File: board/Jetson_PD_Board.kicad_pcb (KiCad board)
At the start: 2 copper layers, 100 x 100.5 mm, 28 parts, among them J1 USB4081-03-A, J2 768250002, Q1 NTTFS5C673NLTAG, Q2 NTTFS5C673NLTAG, Q3 NTTFS5C673NLTAG, U1 APK43070DKZ-13-FA01, U2 USBLC6-2SC6

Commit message: Fixed 3D model file path
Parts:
- moved C7 233.8 mm to (54.0, 265.0)
- moved C8 227.8 mm to (54.1, 261.5)
- moved TH1 224.8 mm to (54.5, 256.5)
- moved R10 221.8 mm to (54.5, 251.0)
- moved R9 219.8 mm to (54.6, 246.5)
- moved R8 217.8 mm to (54.5, 242.0)
- moved C5 211.6 mm to (41.1, 238.5)
- moved C6 211.6 mm to (41.1, 241.0)
- moved R2 211.1 mm to (54.9, 237.5)
- moved C10 209.1 mm to (54.5, 233.0)
- moved C9 206.6 mm to (54.4, 228.0)
- moved R3 205.0 mm to (39.1, 234.5)
- moved C3 202.0 mm to (54.0, 223.0)
- moved R4 201.1 mm to (33.0, 233.0)
- moved C4 194.5 mm to (54.0, 218.0)
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
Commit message: Fixed 3d all 3D model file paths
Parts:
- U1: moved to F.Cu
- moved C7 199.1 mm to (143.5, 87.1)
- moved TH1 195.5 mm to (152.2, 87.1)
- moved C8 193.7 mm to (143.5, 89.6)
- moved R10 192.9 mm to (152.2, 84.6)
- moved R9 191.2 mm to (152.2, 82.1)
- moved R8 189.5 mm to (152.2, 79.6)
- moved C5 186.9 mm to (143.5, 82.1)
- moved C6 186.9 mm to (143.5, 84.6)
- moved R4 185.6 mm to (147.8, 87.1)
- moved R3 185.2 mm to (147.8, 84.6)
- moved R2 181.1 mm to (147.8, 82.1)
- moved C10 179.6 mm to (147.8, 79.6)
- moved C9 177.5 mm to (147.8, 77.1)
- moved C3 171.2 mm to (143.5, 77.1)
- moved C4 164.8 mm to (143.5, 79.6)
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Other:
- board outline removed

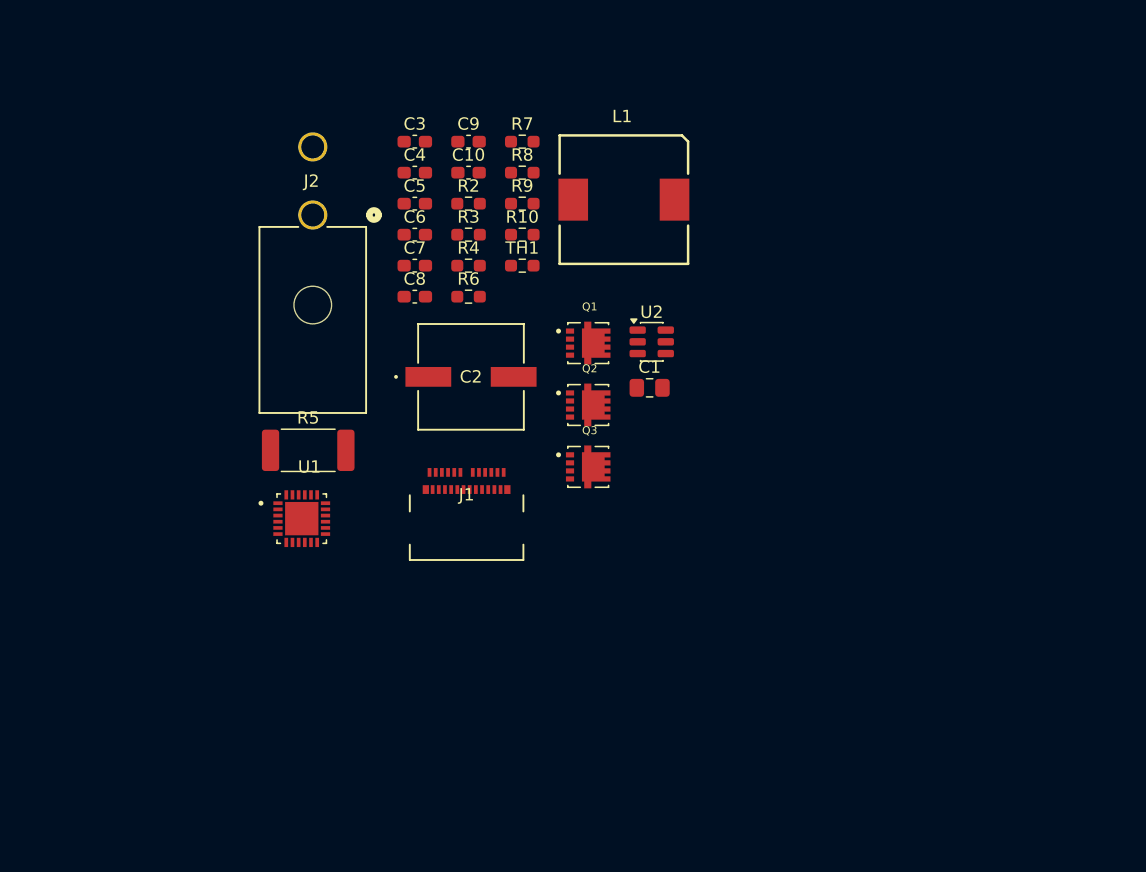
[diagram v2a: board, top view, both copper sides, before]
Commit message: Began placing components
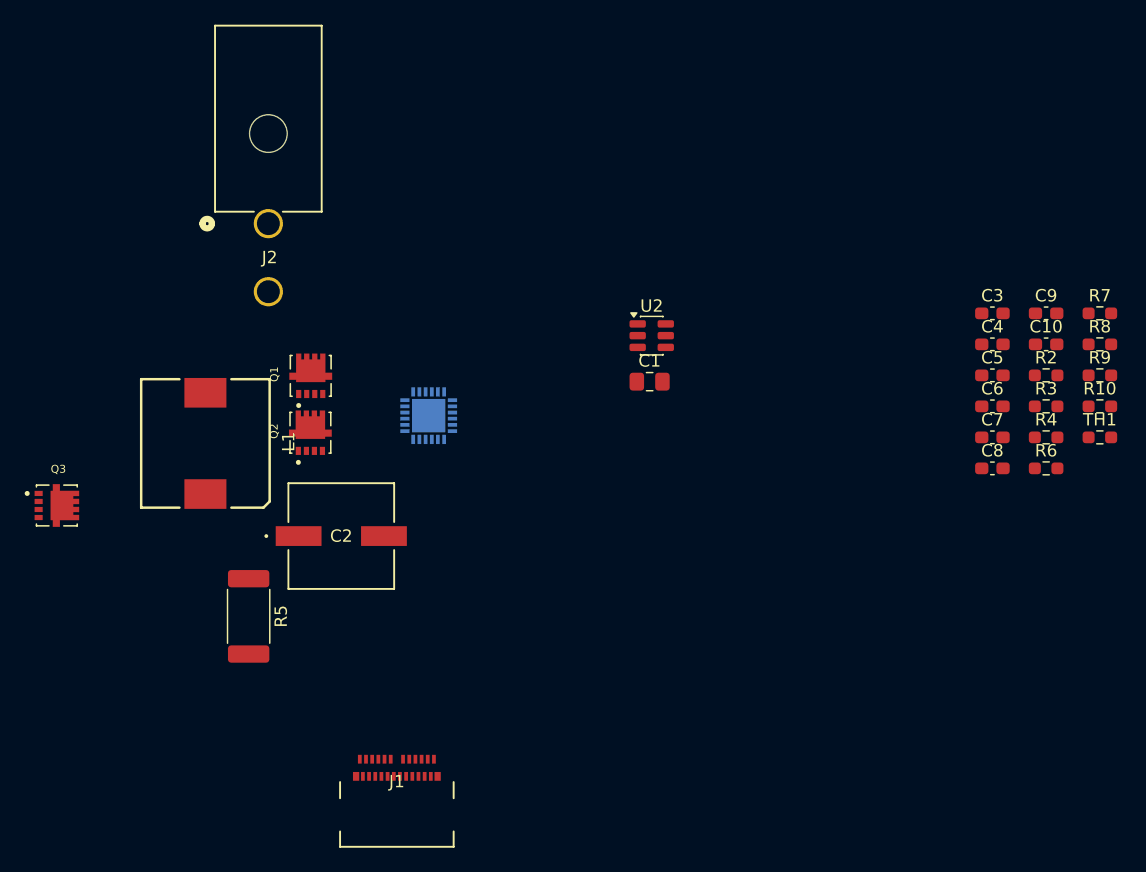
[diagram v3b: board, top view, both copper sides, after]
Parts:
- U1: moved to B.Cu
- moved C3 48.8 mm to (190.2, 91.0)
- moved C4 48.8 mm to (190.2, 93.5)
- moved C5 48.8 mm to (190.2, 96.0)
- moved C6 48.8 mm to (190.2, 98.5)
- moved C7 48.8 mm to (190.2, 101.0)
- moved C8 48.8 mm to (190.2, 103.5)
- moved C10 48.8 mm to (194.6, 93.5)
- moved C9 48.8 mm to (194.6, 91.0)
- moved R10 48.8 mm to (198.9, 98.5)
- moved R2 48.8 mm to (194.6, 96.0)
- moved R3 48.8 mm to (194.6, 98.5)
- moved R4 48.8 mm to (194.6, 101.0)
- moved R6 48.8 mm to (194.6, 103.5)
- moved R7 48.8 mm to (198.9, 91.0)
- moved R8 48.8 mm to (198.9, 93.5)
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
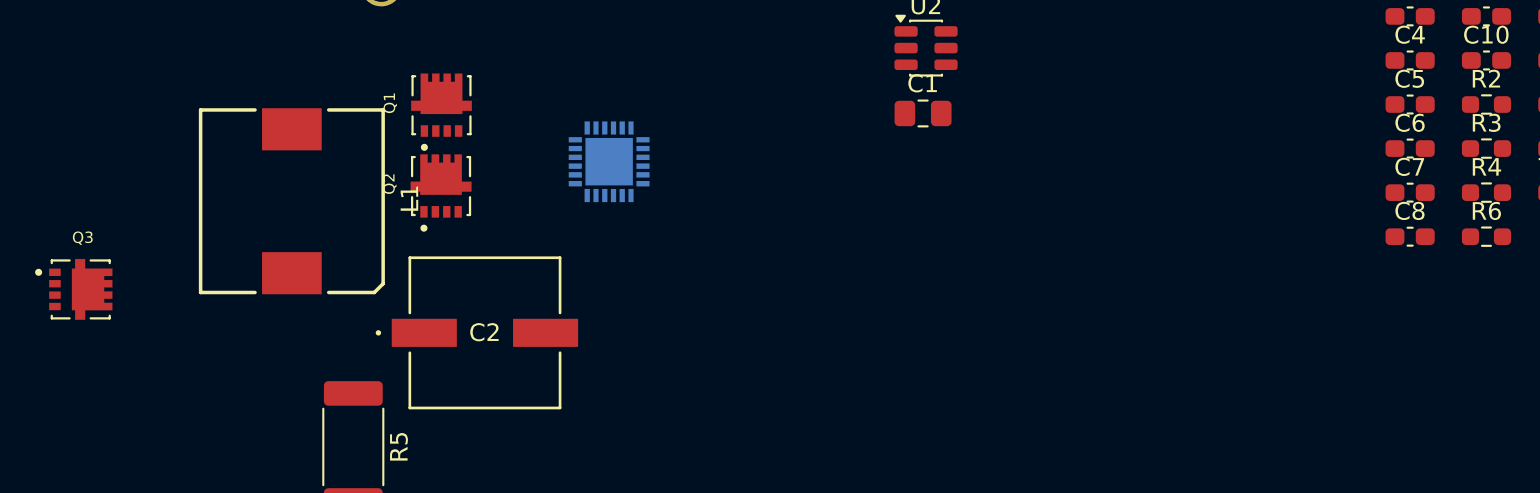
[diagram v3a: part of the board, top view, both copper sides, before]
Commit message: Fixed missing pad gnd
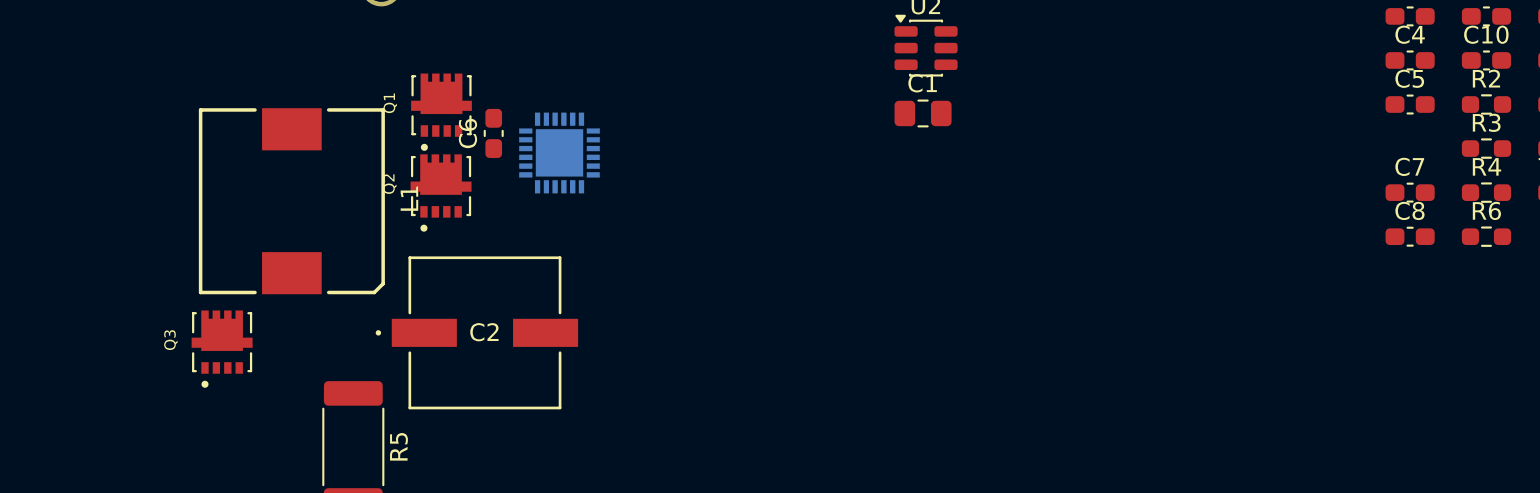
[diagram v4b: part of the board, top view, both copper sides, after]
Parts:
- moved C6 52.2 mm to (138.0, 97.6), turned to 90 degrees
- moved Q3 8.60 mm to (122.5, 109.5), turned to 90 degrees
- moved U1 2.87 mm to (141.8, 98.8)
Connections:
- U1 pad 25: (no net) -> GND
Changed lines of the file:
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@@
 	(footprint "PD_Hardware_Footprints:TRANS_NVTFS5116PLTAG"
 		(layer "F.Cu")
-		(at 114.47 106.525)
+		(at 122.525 109.53 90)
 		(property "Reference" "Q3"
-			(at 0.127 -2.9464 0)
+			(at 0.127 -2.9464 90)
 			(layer "F.SilkS")
 			(effects
@@
 		)
 		(property "Value" "NTTFS5C673NLTAG"
-			(at 6.223 2.7686 0)
+			(at 6.223 2.7686 90)
 			(layer "F.Fab")
 			(effects
@@
 		)
 		(property "Datasheet" "https://www.digikey.com/en/products/detail/onsemi/NTTFS5C673NLTAG/6005173"
-			(at 0 0 0)
+			(at 0 0 90)
 			(layer "F.Fab")
 			(hide yes)
@@
 		)
 		(property "Description" "N-MOSFET transistor, drain/source/gate"
-			(at 0 0 0)
+			(at 0 0 90)
 			(layer "F.Fab")
 			(hide yes)
@@
 		)
 		(property "Sim.Device" "NMOS"
-			(at 0 0 0)
+			(at 0 0 90)
 			(unlocked yes)
 			(layer "F.Fab")
@@
 		)
 		(property "Sim.Type" "VDMOS"
-			(at 0 0 0)
+			(at 0 0 90)
 			(unlocked yes)
 			(layer "F.Fab")
@@
 		)
 		(property "Sim.Pins" "1=D 2=G 3=S"
-			(at 0 0 0)
+			(at 0 0 90)
 			(unlocked yes)
 			(layer "F.Fab")
@@
 		)
 		(fp_line
-			(start -1.65 -1.65)
-			(end -1.65 -1.5)
+			(start 1.65 -1.65)
+			(end 1.65 -1.5)
 			(stroke
 				(width 0.127)
@@
 		)
 		(fp_line
-			(start -1.65 -1.65)
-			(end -0.6335 -1.65)
+			(start 0.5635 -1.65)
+			(end 1.65 -1.65)
 			(stroke
 				(width 0.127)
@@
 		)
 		(fp_line
-			(start -1.65 1.65)
-			(end -1.65 1.5)
+			(start -1.65 -1.65)
+			(end -0.6335 -1.65)
 			(stroke
 				(width 0.127)
@@
 		)
 		(fp_line
-			(start -0.6335 1.65)
-			(end -1.65 1.65)
+			(start -1.65 -1.65)
+			(end -1.65 -1.5)
 			(stroke
 				(width 0.127)
@@
 		)
 		(fp_line
-			(start 0.5635 -1.65)
-			(end 1.65 -1.65)
+			(start 1.65 1.65)
+			(end 1.65 1.5)
 			(stroke
 				(width 0.127)
@@
 		)
 		(fp_line
-			(start 1.65 -1.65)
-			(end 1.65 -1.5)
+			(start 1.65 1.65)
+			(end 0.5635 1.65)
 			(stroke
 				(width 0.127)
@@
 		)
 		(fp_line
-			(start 1.65 1.65)
-			(end 0.5635 1.65)
+			(start -0.6335 1.65)
+			(end -1.65 1.65)
 			(stroke
 				(width 0.127)
@@
 		)
 		(fp_line
-			(start 1.65 1.65)
-			(end 1.65 1.5)
+			(start -1.65 1.65)
+			(end -1.65 1.5)
 			(stroke
 				(width 0.127)
@@
 		)
 		(fp_line
-			(start -2.05 -1.98)
-			(end 2.05 -1.98)
+			(start 2.05 -1.98)
+			(end 2.05 1.98)
 			(stroke
 				(width 0.05)
@@
 		)
 		(fp_line
-			(start -2.05 1.98)
-			(end -2.05 -1.98)
+			(start -2.05 -1.98)
+			(end 2.05 -1.98)
 			(stroke
 				(width 0.05)
@@
 		)
 		(fp_line
-			(start 2.05 -1.98)
-			(end 2.05 1.98)
+			(start 2.05 1.98)
+			(end -2.05 1.98)
 			(stroke
 				(width 0.05)
@@
 		)
 		(fp_line
-			(start 2.05 1.98)
-			(end -2.05 1.98)
+			(start -2.05 1.98)
+			(end -2.05 -1.98)
 			(stroke
 				(width 0.05)
@@
 		)
 		(fp_line
-			(start -1.65 -1.65)
-			(end 1.65 -1.65)
+			(start 1.65 -1.65)
+			(end 1.65 1.65)
 			(stroke
 				(width 0.127)
@@
 		)
 		(fp_line
-			(start -1.65 1.65)
-			(end -1.65 -1.65)
+			(start -1.65 -1.65)
+			(end 1.65 -1.65)
 			(stroke
 				(width 0.127)
@@
 		)
 		(fp_line
-			(start 1.65 -1.65)
-			(end 1.65 1.65)
+			(start 1.65 1.65)
+			(end -1.65 1.65)
 			(stroke
 				(width 0.127)
@@
 		)
 		(fp_line
-			(start 1.65 1.65)
-			(end -1.65 1.65)
+			(start -1.65 1.65)
+			(end -1.65 -1.65)
 			(stroke
 				(width 0.127)
@@
 		)
 		(pad "1" smd custom
-			(at 0.635 0)
+			(at 0.635 0 90)
 			(size 0.635 1.27)
 			(layers "F.Cu")
@@
 		)
 		(pad "2" smd rect
-			(at -1.47 0.975)
+			(at -1.47 0.975 90)
 			(size 0.66 0.42)
 			(layers "F.Cu" "F.Mask")
@@
 		)
 		(pad "3" smd rect
-			(at -1.47 -0.975)
+			(at -1.47 -0.975 90)
 			(size 0.66 0.42)
 			(layers "F.Cu" "F.Mask")
@@
 		)
 		(pad "3" smd rect
-			(at -1.47 -0.325)
+			(at -1.47 -0.325 90)
 			(size 0.66 0.42)
 			(layers "F.Cu" "F.Mask")
@@
 		)
 		(pad "3" smd rect
-			(at -1.47 0.325)
+			(at -1.47 0.325 90)
 			(size 0.66 0.42)
 			(layers "F.Cu" "F.Mask")
@@
 	(footprint "Capacitor_SMD:C_0603_1608Metric_Pad1.08x0.95mm_HandSolder"
 		(layer "F.Cu")
-		(at 190.2125 98.5)
+		(at 138 97.6375 90)
 		(descr "Capacitor SMD 0603 (1608 Metric), square (rectangular) end terminal, IPC-7351 nominal with elongated pad for handsoldering. (Body size source: IPC-SM-782 page 76, https://www.pcb-3d.com/wordpress/wp-content/uploads/ipc-sm-782a_amendment_1_and_2.pdf), generated with kicad-footprint-generator")
 		(tags "capacitor handsolder")
 		(property "Reference" "C6"
-			(at 0 -1.43 0)
+			(at 0 -1.43 90)
 			(layer "F.SilkS")
 			(effects
@@
 		)
 		(property "Value" "150nF"
-			(at 0 1.43 0)
+			(at 0 1.43 90)
 			(layer "F.Fab")
 			(effects
@@
 		)
 		(property "Datasheet" "https://www.digikey.com/en/products/detail/tdk-corporation/CGA3E3X7R1V154K080AB/3949785"
-			(at 0 0 0)
+			(at 0 0 90)
 			(layer "F.Fab")
 			(hide yes)
@@
 		)
 		(property "Description" "Unpolarized capacitor"
-			(at 0 0 0)
+			(at 0 0 90)
 			(layer "F.Fab")
 			(hide yes)
@@
 		)
 		(fp_line
-			(start -1.65 -0.73)
-			(end 1.65 -0.73)
+			(start 1.65 -0.73)
+			(end 1.65 0.73)
 			(stroke
 				(width 0.05)
@@
 		)
 		(fp_line
-			(start -1.65 0.73)
-			(end -1.65 -0.73)
+			(start -1.65 -0.73)
+			(end 1.65 -0.73)
 			(stroke
 				(width 0.05)
@@
 		)
 		(fp_line
-			(start 1.65 -0.73)
-			(end 1.65 0.73)
+			(start 1.65 0.73)
+			(end -1.65 0.73)
 			(stroke
 				(width 0.05)
@@
 		)
 		(fp_line
-			(start 1.65 0.73)
-			(end -1.65 0.73)
+			(start -1.65 0.73)
+			(end -1.65 -0.73)
 			(stroke
 				(width 0.05)
@@
 		)
 		(fp_line
-			(start -0.8 -0.4)
-			(end 0.8 -0.4)
+			(start 0.8 -0.4)
+			(end 0.8 0.4)
 			(stroke
 				(width 0.1)
@@
 		)
 		(fp_line
-			(start -0.8 0.4)
-			(end -0.8 -0.4)
+			(start -0.8 -0.4)
+			(end 0.8 -0.4)
 			(stroke
 				(width 0.1)
@@
 		)
 		(fp_line
-			(start 0.8 -0.4)
-			(end 0.8 0.4)
+			(start 0.8 0.4)
+			(end -0.8 0.4)
 			(stroke
 				(width 0.1)
@@
 		)
 		(fp_line
-			(start 0.8 0.4)
-			(end -0.8 0.4)
+			(start -0.8 0.4)
+			(end -0.8 -0.4)
 			(stroke
 				(width 0.1)
@@
 		)
 		(fp_text user "${REFERENCE}"
-			(at 0 0 0)
+			(at 0 0 90)
 			(layer "F.Fab")
 			(effects
@@
 		)
 		(pad "1" smd roundrect
-			(at -0.8625 0)
+			(at -0.8625 0 90)
 			(size 1.075 0.95)
 			(layers "F.Cu" "F.Mask" "F.Paste")
@@
 		)
 		(pad "2" smd roundrect
-			(at 0.8625 0)
+			(at 0.8625 0 90)
 			(size 1.075 0.95)
 			(layers "F.Cu" "F.Mask" "F.Paste")
@@
 	(footprint "PD_Hardware_Footprints:IC_AP33771DKZ-13"
 		(layer "B.Cu")
-		(at 144.575 99.25 180)
+		(at 141.75 98.75 180)
 		(property "Reference" "U1"
 			(at 0.625 4.185 0)
@@
 			(size 2.7 2.7)
 			(layers "B.Cu" "B.Mask")
+			(net 1 "GND")
+			(pinfunction "PAD")
+			(pintype "power_in")
 			(solder_mask_margin 0.102)
 		)
